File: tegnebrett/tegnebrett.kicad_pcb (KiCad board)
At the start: 2 copper layers, 203 parts, among them J1 FH12-45S-0.5SH55, J2 FH12-6S-1SH55, J3 Conn_ST_STDC14, J4 USB-A1HSW6, J5 MCU_Header_Pin, J6 FPGA_debug1, J7 FPGA_Header_Pin, J8 DA15_Socket, J9 PJ-002A, SW1 SW_Push, SW2 SW_Push, SW3 MCU_Button, SW4 Reset, SW5 Undo, SW6 FPGA_Button, U1 STM32U5G7VJTxQ, U2 XC7A100T-2FTG256I, U3 Oscillator 100MHz, U4 IS66WVH16M8DBLL-100B1LI1, U5 VGA Transceiver, U6 VGA Transciever, U7 TPS54294PWP2, U8 TPS54294PWP1, Y1 48MHz

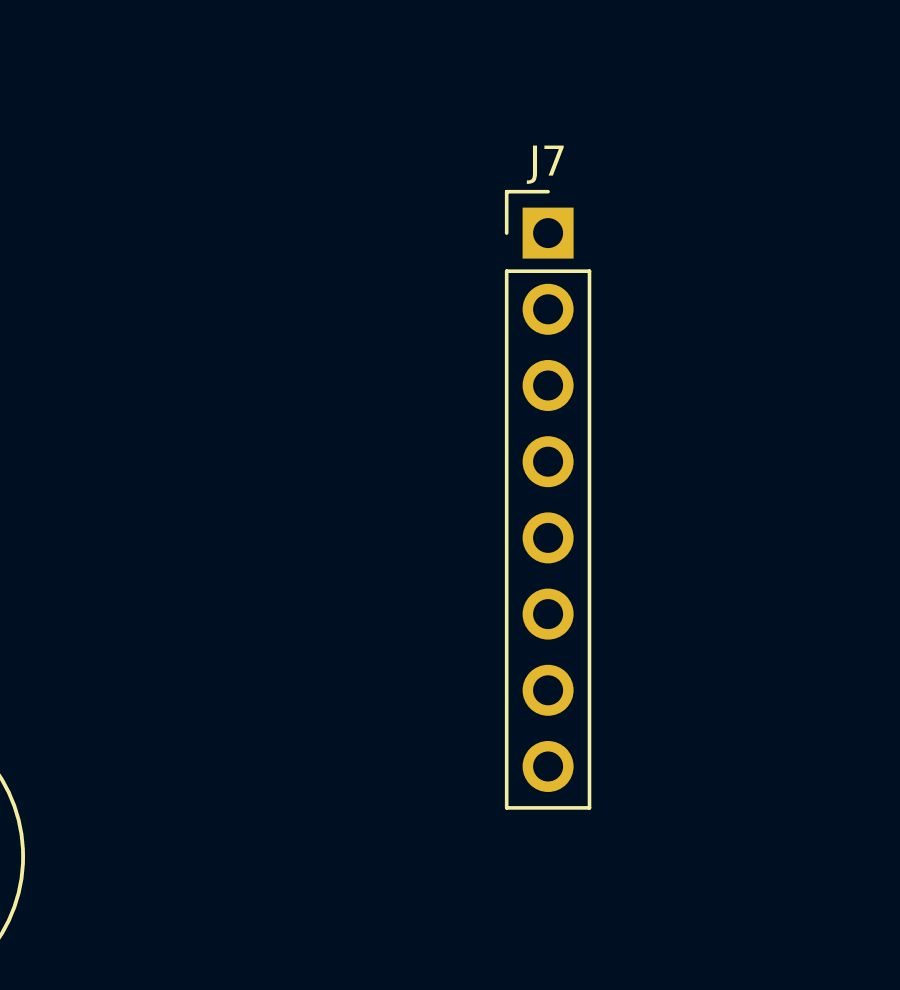
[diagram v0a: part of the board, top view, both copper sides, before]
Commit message: refactor: rename project from getting-started to tegnebrett
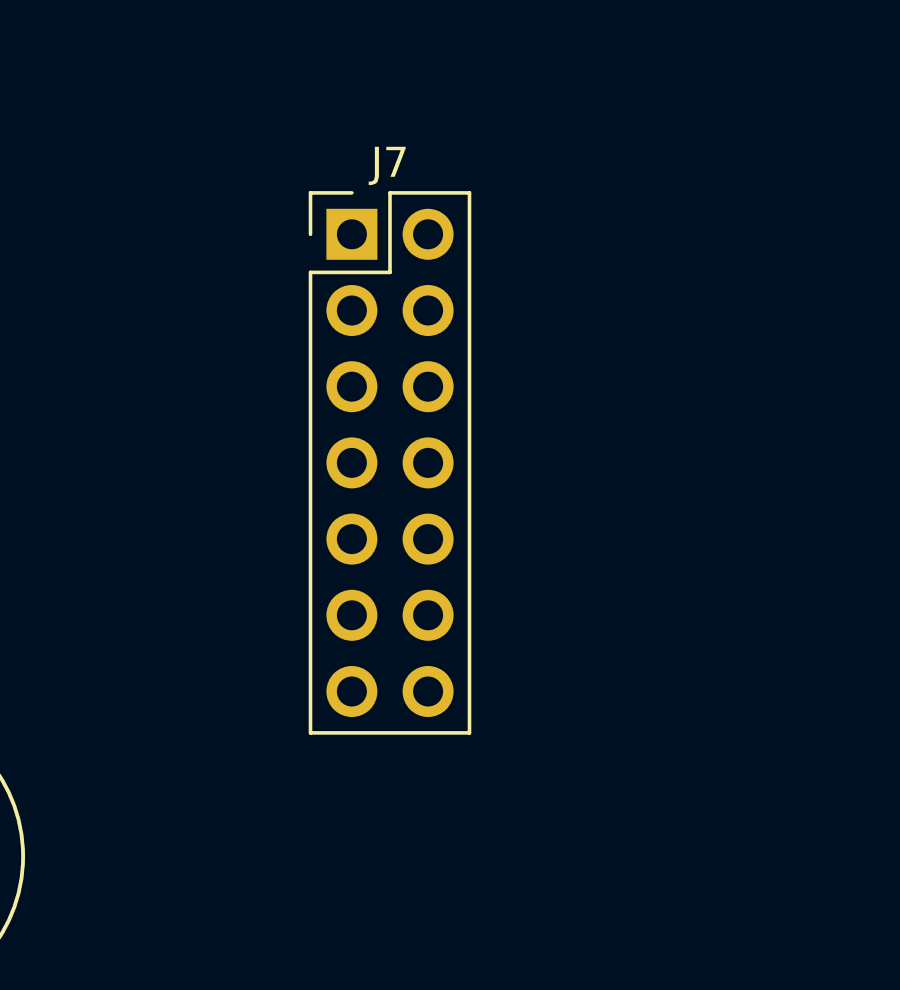
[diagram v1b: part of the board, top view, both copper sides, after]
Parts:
- J7: footprint Connector_PinHeader_2.54mm:PinHeader_1x08_P2.54mm_Vertical -> Connector_PinHeader_2.54mm:PinHeader_2x07_P2.54mm_Vertical
- moved J7 6.54 mm to (189.5, 14.8)
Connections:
- J7 pad 1: /FPGA/Header1 -> +3V3
- J7 pad 2: /FPGA/Header2 -> GND
- J7 pad 3: /FPGA/Header3 -> /FPGA/Header2
- J7 pad 4: /FPGA/Header4 -> /FPGA/Header1
- J7 pad 5: /FPGA/Header5 -> /FPGA/Header4
- J7 pad 6: /FPGA/Header6 -> /FPGA/Header3
- J7 pad 7: +3V3 -> /FPGA/Header6
- J7 pad 8: GND -> /FPGA/Header5
- U2 pad A10: unconnected-(U2A-IO_L3N_T0_DQS_AD1N_15-PadA10) -> /FPGA/Header7
- U2 pad B10: unconnected-(U2A-IO_L4P_T0_15-PadB10) -> /FPGA/Header8
- U2 pad B11: unconnected-(U2A-IO_L4N_T0_15-PadB11) -> /FPGA/Header9
- U2 pad B12: unconnected-(U2A-IO_L5P_T0_AD9P_15-PadB12) -> /FPGA/Header10
- U5 pad 10: (no net) -> GND
- U6 pad 10: (no net) -> GND

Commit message: superfeat: PCB updates from Tormod
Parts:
- C10, C11, C12, C13, C14, C15, C16, C17, C27, C28, C29, C30, C31, C32, C33, C34, C35, C36, C37, C38, C39, C40, C41, C42, C43, C44, C45, C46, C47, C48, C49, C5, C50, C51, C52, C53, C54, C55, C56, C57, C58, C59, C6, C60, C61, C62, C63, C64, C7, C8, C9, L1: moved to B.Cu
- moved J7 187.4 mm to (147.0, 197.3)
- moved J3 162.0 mm to (137.7, 245.7)
- moved J5 162.0 mm to (138.0, 239.7)
- moved J6 162.0 mm to (135.0, 197.4)
- moved R11 162.0 mm to (143.5, 255.0)
- moved R12 162.0 mm to (143.5, 245.6)
- moved R13 162.0 mm to (143.5, 248.6)
- moved R14 162.0 mm to (143.5, 251.5)
- moved R15 162.0 mm to (128.5, 196.1)
- moved R16 162.0 mm to (128.5, 199.0)
- moved R17 162.0 mm to (128.0, 203.6)
- moved R18 162.0 mm to (128.0, 206.5)
- moved R19 162.0 mm to (128.0, 210.5)
- moved R2 162.0 mm to (113.0, 195.0)
- moved R27 162.0 mm to (214.5, 219.5)
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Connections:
- C69 pad 1: Net-(U7-EN1) -> POWER_IN
- C71 pad 1: Net-(U7-EN1) -> POWER_IN
- C80 pad 1: Net-(U7-EN1) -> POWER_IN
- C82 pad 1: Net-(U7-EN1) -> POWER_IN
- J9 pad 3: Net-(U7-EN1) -> POWER_IN
- U7 pad 1: Net-(U7-EN1) -> POWER_IN
- U7 pad 16: Net-(U7-EN1) -> POWER_IN
- U7 pad 5: Net-(U7-EN1) -> POWER_IN
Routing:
- net +3V3: track 0.00 -> 201.0 mm, vias 0 -> 20
- net /TOUCH_SDA: track 0.00 -> 82.2 mm, vias 0 -> 2
- net /TOUCH_SCL: track 0.00 -> 79.5 mm, vias 0 -> 2
- net +1V0: track 0.00 -> 71.3 mm, vias 0 -> 5
- net /TOUCH_WAKE: track 0.00 -> 65.1 mm, vias 0 -> 2
- net /R2: track 0.00 -> 63.8 mm
- net /G3: track 0.00 -> 63.1 mm, vias 0 -> 2
- net /VSYNC: track 0.00 -> 61.7 mm, vias 0 -> 2
- net /G2: track 0.00 -> 59.9 mm, vias 0 -> 2
- net /LCD_RESET: track 0.00 -> 59.3 mm, vias 0 -> 2
- net /B3: track 0.00 -> 58.8 mm, vias 0 -> 2
- net /B2: track 0.00 -> 58.7 mm, vias 0 -> 2
- net /TOUCH_INT: track 0.00 -> 58.6 mm, vias 0 -> 2
- net /B7: track 0.00 -> 58.6 mm, vias 0 -> 2
- net /G4: track 0.00 -> 58.2 mm, vias 0 -> 2
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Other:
- copper layers 2 -> 6

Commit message: superfeat: complete PCBv0.1
Tormod has done a great job!
Now we're done for the day.
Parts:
- J6: value FPGA_debug1 -> FPGA_debug
- R17, R18, R19, R23, R24: moved to B.Cu
- moved J9 259.0 mm to (238.0, 51.5), turned to 0 degrees
- moved JP4 237.9 mm to (230.8, 53.0)
- moved J3 233.5 mm to (162.3, 13.5), turned to -90 degrees
- moved JP3 231.6 mm to (236.2, 66.2), turned to 180 degrees
- moved J5 226.3 mm to (149.7, 13.8), turned to -90 degrees
- moved R11 221.9 mm to (161.0, 33.8), turned to -90 degrees
- moved R14 218.2 mm to (157.0, 33.8), turned to -90 degrees
- moved R13 215.4 mm to (159.0, 33.8), turned to -90 degrees
- moved R12 212.7 mm to (163.0, 33.8), turned to -90 degrees
- moved C81 209.7 mm to (218.2, 63.2), turned to 90 degrees
- moved C79 208.2 mm to (214.8, 63.8), turned to 90 degrees
- moved C70 206.8 mm to (209.2, 61.8), turned to 90 degrees
- moved R75 205.4 mm to (231.8, 71.0), turned to -90 degrees
- moved R76 205.3 mm to (231.8, 75.5), turned to -90 degrees
- moved C72 204.7 mm to (205.5, 62.0), turned to 90 degrees
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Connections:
- R27 pad 2: Net-(U2A-IO_L19N_T3_A21_VREF_15) -> Net-(U2A-IO_L7P_T1_AD2P_15)
- SW4 pad 1: Net-(U1-PC9) -> GND
- SW4 pad 3: (no net) -> Net-(U1-PC9)
- SW5 pad 3: (no net) -> Net-(U1-PC15)
- SW6 pad 1: Net-(U2A-IO_L19N_T3_A21_VREF_15) -> Net-(U2A-IO_L7P_T1_AD2P_15)
- U2 pad A12: unconnected-(U2A-IO_L5N_T0_AD9N_15-PadA12) -> /FPGA/DQ0
- U2 pad A13: unconnected-(U2A-IO_L7P_T1_AD2P_15-PadA13) -> Net-(U2A-IO_L7P_T1_AD2P_15)
- U2 pad G12: Net-(U2A-IO_L19N_T3_A21_VREF_15) -> unconnected-(U2A-IO_L19N_T3_A21_VREF_15-PadG12)
- U2 pad H12: /FPGA/DQ0 -> unconnected-(U2A-IO_L20P_T3_A20_15-PadH12)
- U2 pad N11: /SCK_FPGA -> unconnected-(U2A-IO_L13P_T2_MRCC_14-PadN11)
- U2 pad N14: unconnected-(U2A-IO_L12P_T1_MRCC_14-PadN14) -> /SCK_FPGA
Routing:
- net +3V3: track 201.0 -> 982.0 mm, vias 20 -> 48
- net GND: track 10.3 -> 569.8 mm, vias 1 -> 98
- net POWER_IN: track 0.00 -> 244.4 mm, vias 0 -> 2
- net +1V8: track 28.6 -> 188.7 mm
- net +5V: track 0.00 -> 136.9 mm, vias 0 -> 2
- net +1V0: track 71.3 -> 171.3 mm
- net /DEBUG_SWO: track 0.00 -> 91.0 mm, vias 0 -> 2
- net /MISO_FPGA: track 0.00 -> 87.5 mm, vias 0 -> 4
- net /INTERRUPT: track 0.00 -> 87.3 mm, vias 0 -> 5
- net /MOSI_FPGA: track 0.00 -> 79.5 mm, vias 0 -> 4
- net /CS_FPGA: track 0.00 -> 78.6 mm, vias 0 -> 4
- net /FPGA/VGA/B2: track 0.00 -> 77.4 mm, vias 0 -> 2
- net /DEBUG_JTRST: track 0.00 -> 76.8 mm, vias 0 -> 2
- net /FPGA/VGA/B0: track 0.00 -> 76.7 mm, vias 0 -> 2
- net /FPGA/VGA/B3: track 0.00 -> 76.6 mm, vias 0 -> 2
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- added copper zone on In3.Cu, net GND
